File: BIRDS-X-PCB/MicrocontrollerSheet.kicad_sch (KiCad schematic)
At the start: 30 parts, among them J401 Conn_02x04_Odd_Even, J402 Conn_01x08, Q401 BSS138, Q402 BSS138, SW401 SW_Push, U401 STM32G031K8Tx, U402 MTT4B-Mini, U403 MT29F2G01ABAGDWB-IT-G_TR, Y401 ECS-2520SMV-080-FN-TR

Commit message: Add notes from schematic review session
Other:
- note added: "TODO breakout ~3 GPIOs, add debug LED"
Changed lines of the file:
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@@
+    (effects (font (size 1.27 1.27)) (justify left bottom))
+  )
+  (text "TODO breakout ~3 GPIOs, add debug LED" (at 184.15 102.87 0)
     (effects (font (size 1.27 1.27)) (justify left bottom))
   )

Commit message: Finish layout
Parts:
- added D203: LED, LED_SMD:LED_1206_3216Metric_Pad1.42x1.75mm_HandSolder, symbol Device:LED
- added J403: Conn_01x02, Connector_PinHeader_2.54mm:PinHeader_1x02_P2.54mm_Vertical, symbol Connector_Generic:Conn_01x02
- added J404: MHDR2X5, Connector_PinHeader_1.27mm:PinHeader_2x05_P1.27mm_Vertical_SMD, symbol Connector_Generic:Conn_02x05_Odd_Even
- added R205: R, Resistor_SMD:R_0805_2012Metric_Pad1.20x1.40mm_HandSolder, symbol Device:R
- C401, C402, C403, C404, C405, C406, C407, C408: footprint Capacitor_SMD:C_1206_3216Metric_Pad1.33x1.80mm_HandSolder -> Capacitor_SMD:C_0805_2012Metric_Pad1.18x1.45mm_HandSolder
- J401: value Conn_02x04_Odd_Even -> Conn_01x04; footprint Connector_PinSocket_2.54mm:PinSocket_2x04_P2.54mm_Vertical -> Connector_PinHeader_2.54mm:PinHeader_1x04_P2.54mm_Vertical; symbol Connector_Generic:Conn_02x04_Odd_Even -> Connector_Generic:Conn_01x04
- R401, R402, R403, R404, R405, R406, R407, R408, R409: footprint Resistor_SMD:R_1206_3216Metric_Pad1.30x1.75mm_HandSolder -> Resistor_SMD:R_0805_2012Metric_Pad1.20x1.40mm_HandSolder
- TP401: footprint TestPoint:TestPoint_Pad_D2.5mm -> TestPoint:TestPoint_Pad_D2.0mm
- U402: footprint BIRDS-X_Footprints_Lib:MTT4B-Mini -> BIRDS-X_Footprints_Lib:MTT4B-Mini_CanUp
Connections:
- net +3V3: now also J404.1 (Pin_1)
- net +5V: now also J401.3 (Pin_3); no longer J401.5 (Pin_5), J401.6 (Pin_6)
- net BOOT0: now also J404.4 (Pin_4)
- net GND: now also D203.1 (K), J404.3 (Pin_3), J404.5 (Pin_5), J404.9 (Pin_9); no longer J401.2 (Pin_2)
- net at JP403.1 (A), Q401.3 (D), R405.2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: now also J401.2 (Pin_2); no longer J401.3 (Pin_3), J401.4 (Pin_4)
- net at JP404.1 (A), Q402.3 (D), R406.2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: now also J401.4 (Pin_4); no longer J401.7 (Pin_7), J401.8 (Pin_8)
- net ST_RST: now reaches C401.1, SW401.2, U401.6 (PF2)
- net ST_RST: now also J404.10 (Pin_10)
- net at U401.22 (PA11/PA9): now also R205.1
- net at U401.23 (PA12/PA10): now also J403.1 (Pin_1)
- net ST_SWDIO: now reaches U401.24 (PA13)
- net ST_SWDIO: now also J404.2 (Pin_2)
- net at U401.26 (PA15): now also J403.2 (Pin_2)
- new net: D203.2 (A), R205.2
- no-connect marks 10 -> 9
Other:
- note added: "Breakout (at 5V logic)"
- note added: "Debugging"
- note added: "GP Debugging Breakout"
- note added: "ST-LINK/V2 Connector for Programming"
- note removed: "TODO add programming header from Iris schematic"
- note removed: "TODO breakout ~3 GPIOs, add debug LED"

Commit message: PCB update
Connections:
- net +3V3: no longer C404.1
- net GND: no longer C404.2
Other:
- moved on the sheet: C404
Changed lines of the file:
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@@
     )
   )
-  (symbol (lib_id "Device:C") (at 33.02 92.71 0) (unit 1)
+  (symbol (lib_id "Device:C") (at 33.02 92.71 90) (unit 1)
     (in_bom yes) (on_board yes) (dnp no)
-    (property "Reference" "C404" (at 35.56 91.44 0)
+    (property "Reference" "C404" (at 31.75 90.17 0)
       (effects (font (size 1.27 1.27)) (justify left))
     )
-    (property "Value" "10n" (at 35.56 93.98 0)
+    (property "Value" "10n" (at 34.29 90.17 0)
       (effects (font (size 1.27 1.27)) (justify left))
     )
-    (property "Footprint" "Capacitor_SMD:C_0805_2012Metric_Pad1.18x1.45mm_HandSolder" (at 33.9852 96.52 0)
+    (property "Footprint" "Capacitor_SMD:C_0805_2012Metric_Pad1.18x1.45mm_HandSolder" (at 36.83 91.7448 0)
       (effects (font (size 1.27 1.27)) hide)
     )

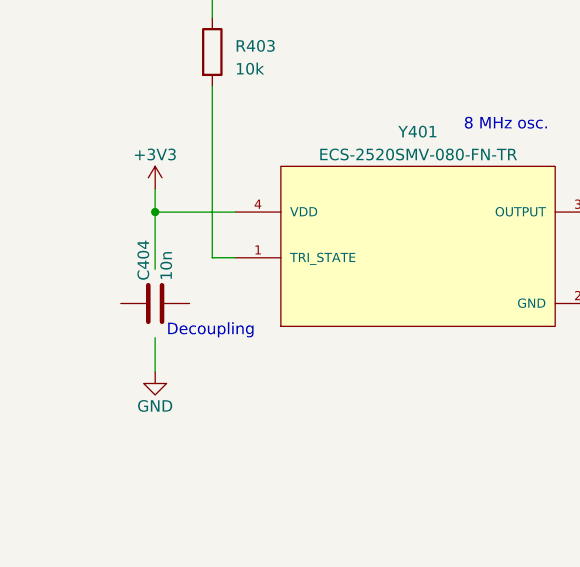
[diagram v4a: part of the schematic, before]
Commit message: Route power lines on 2-layer board, if desired
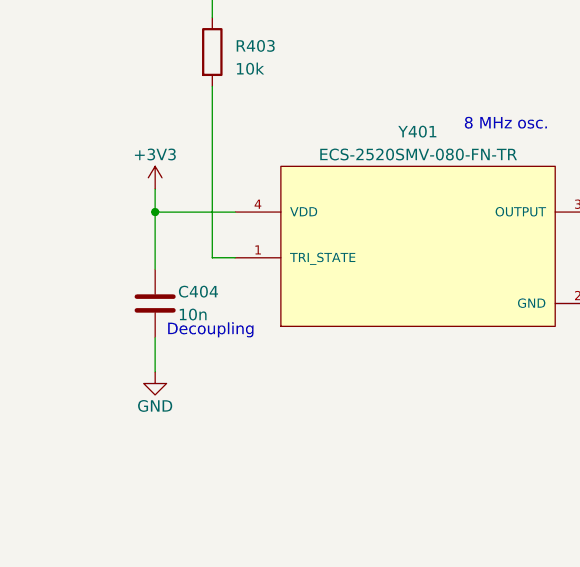
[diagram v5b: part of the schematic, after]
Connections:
- net +3V3: now also C404.1
- net GND: now also C404.2
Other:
- moved on the sheet: C404
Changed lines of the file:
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@@
     )
   )
-  (symbol (lib_id "Device:C") (at 33.02 92.71 90) (unit 1)
+  (symbol (lib_id "Device:C") (at 33.02 92.71 0) (unit 1)
     (in_bom yes) (on_board yes) (dnp no)
-    (property "Reference" "C404" (at 31.75 90.17 0)
+    (property "Reference" "C404" (at 35.56 91.44 0)
       (effects (font (size 1.27 1.27)) (justify left))
     )
-    (property "Value" "10n" (at 34.29 90.17 0)
+    (property "Value" "10n" (at 35.56 93.98 0)
       (effects (font (size 1.27 1.27)) (justify left))
     )
-    (property "Footprint" "Capacitor_SMD:C_0805_2012Metric_Pad1.18x1.45mm_HandSolder" (at 36.83 91.7448 0)
+    (property "Footprint" "Capacitor_SMD:C_0805_2012Metric_Pad1.18x1.45mm_HandSolder" (at 33.9852 96.52 0)
       (effects (font (size 1.27 1.27)) hide)
     )

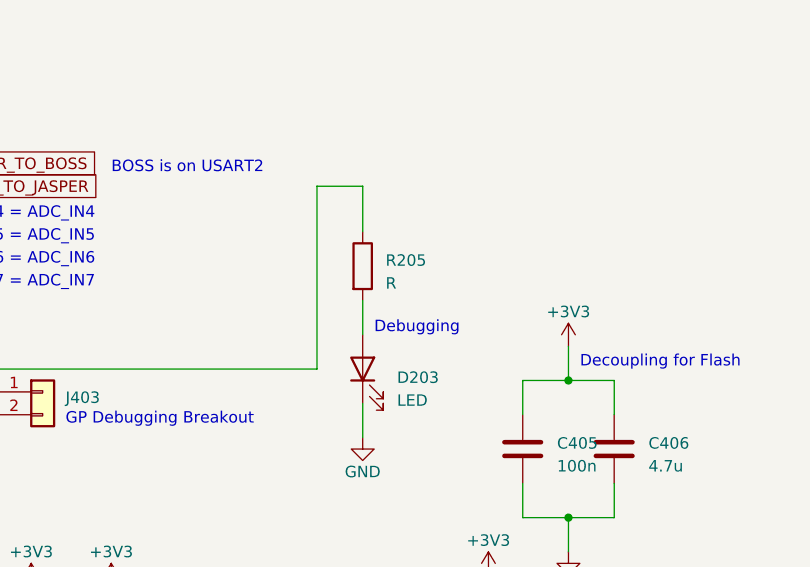
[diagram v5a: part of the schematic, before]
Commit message: Update resistor vals, plot, BOM
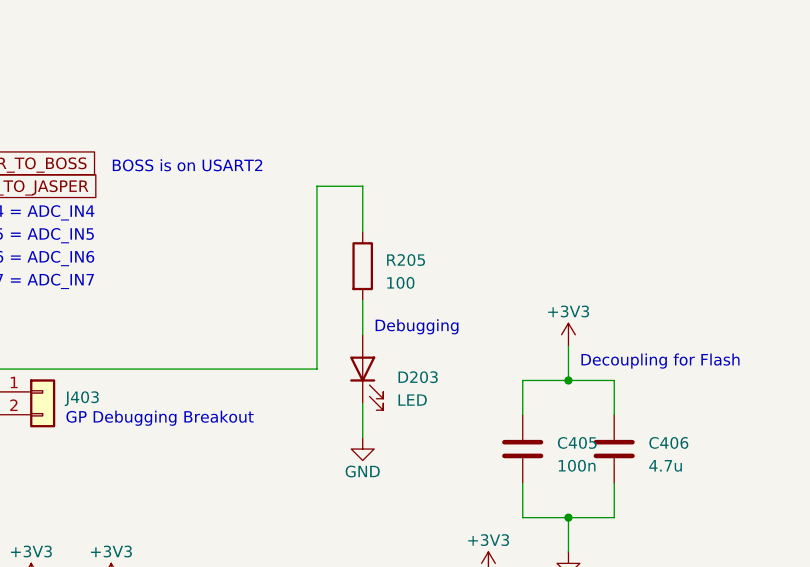
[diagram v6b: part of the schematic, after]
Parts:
- J402: footprint Connector_PinSocket_2.54mm:PinSocket_1x08_P2.54mm_Vertical -> Connector_PinHeader_2.54mm:PinHeader_1x08_P2.54mm_Vertical
- R205: value R -> 100
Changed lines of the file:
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@@
       (effects (font (size 1.27 1.27)) (justify left) hide)
     )
-    (property "Footprint" "Connector_PinSocket_2.54mm:PinSocket_1x08_P2.54mm_Vertical" (at 245.11 143.51 0)
+    (property "Footprint" "Connector_PinHeader_2.54mm:PinHeader_1x08_P2.54mm_Vertical" (at 245.11 143.51 0)
       (effects (font (size 1.27 1.27)) hide)
     )
@@
       (effects (font (size 1.27 1.27)) (justify left))
     )
-    (property "Value" "R" (at 220.98 93.345 0)
+    (property "Value" "100" (at 220.98 93.345 0)
       (effects (font (size 1.27 1.27)) (justify left))
     )

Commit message: Final changes for rev1
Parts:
- SW401: footprint Button_Switch_SMD:SW_Push_SPST_NO_Alps_SKRK -> Button_Switch_SMD:SW_Tactile_SPST_NO_Straight_CK_PTS636Sx25SMTRLFS
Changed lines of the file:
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@@
       (effects (font (size 1.27 1.27)) (justify right))
     )
-    (property "Footprint" "Button_Switch_SMD:SW_Push_SPST_NO_Alps_SKRK" (at 91.44 64.77 0)
+    (property "Footprint" "Button_Switch_SMD:SW_Tactile_SPST_NO_Straight_CK_PTS636Sx25SMTRLFS" (at 91.44 64.77 0)
       (effects (font (size 1.27 1.27)) hide)
     )

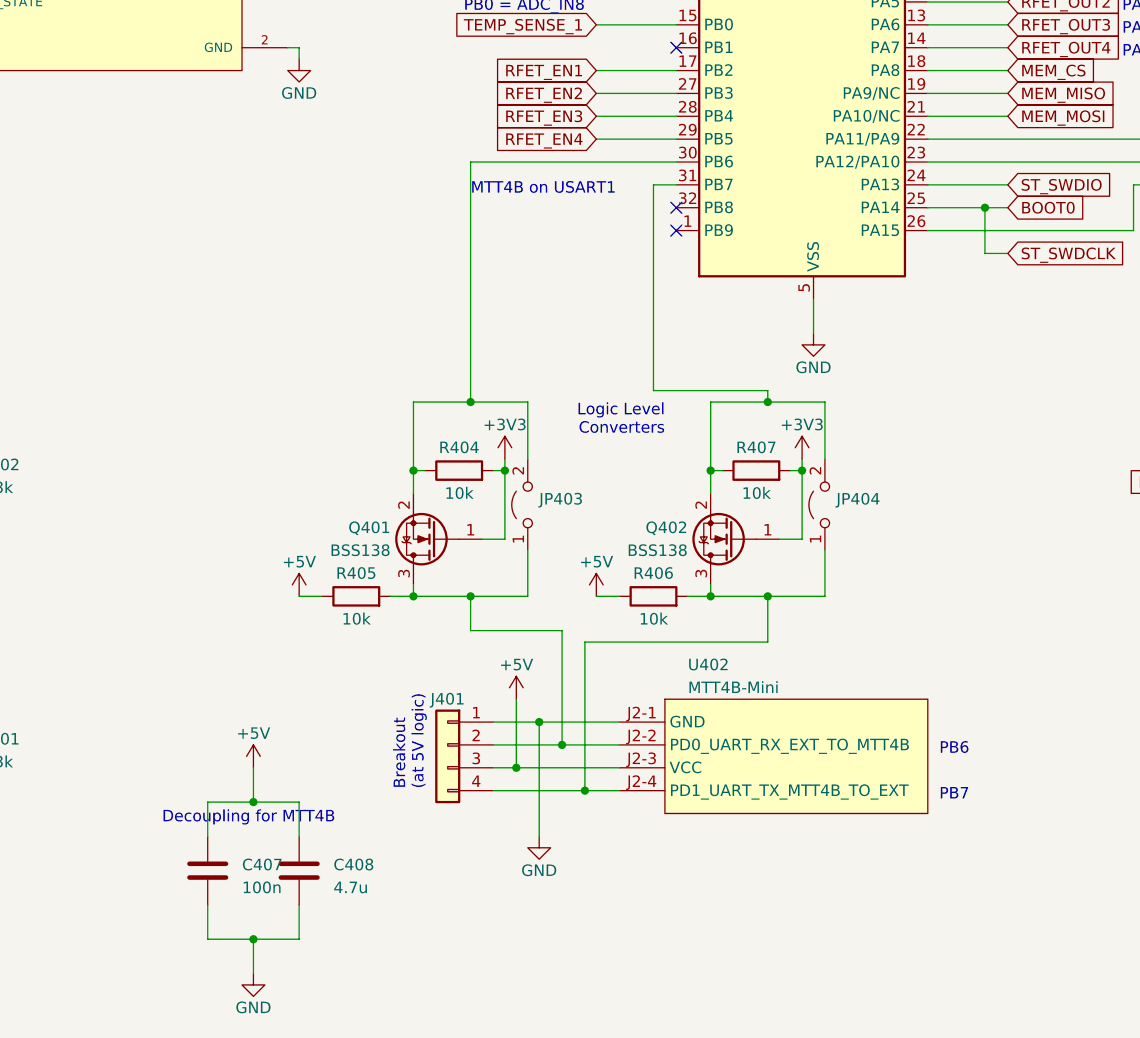
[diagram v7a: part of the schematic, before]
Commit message: Update footprints to 0603
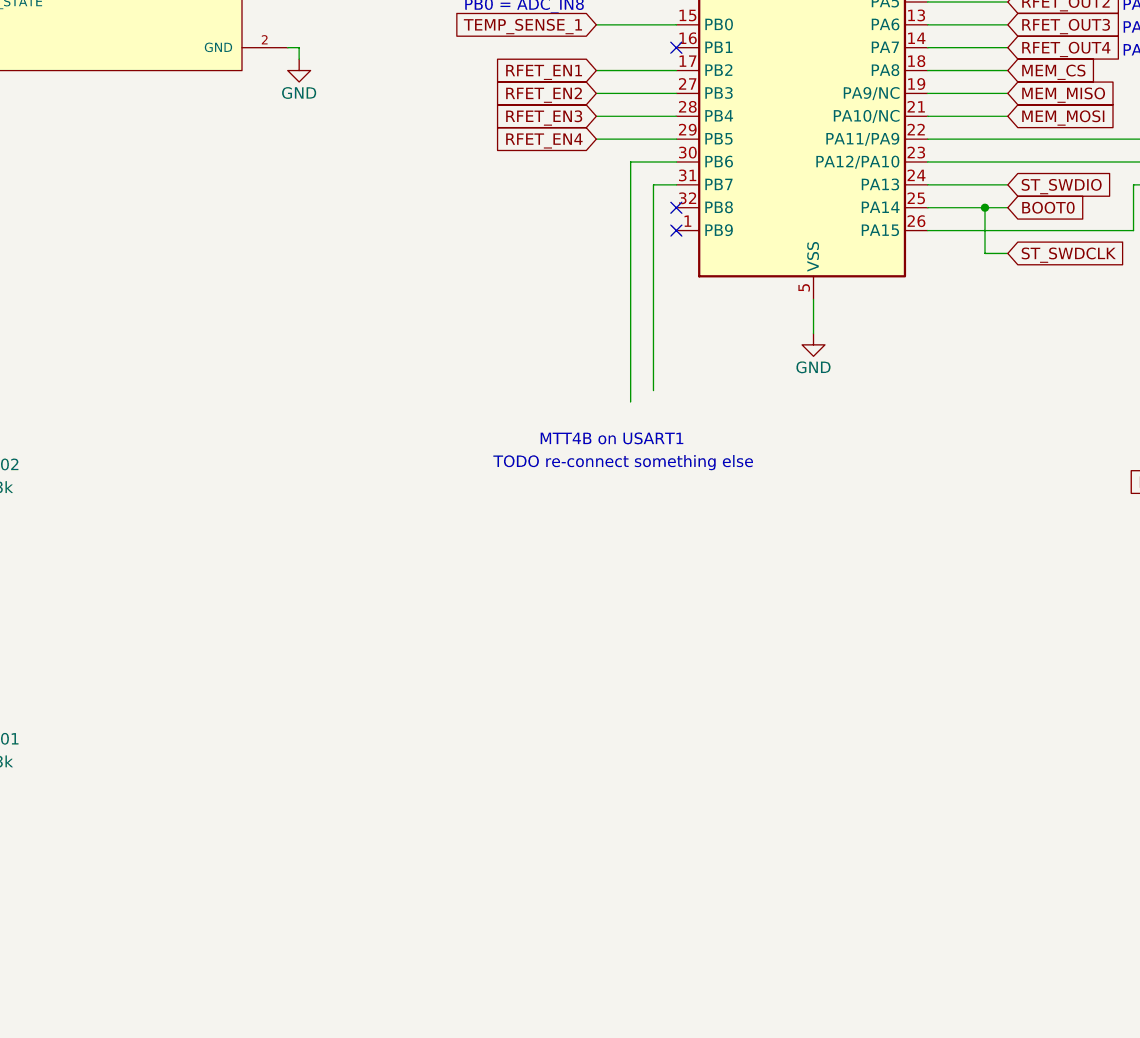
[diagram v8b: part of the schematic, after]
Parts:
- removed C407: 100n, Capacitor_SMD:C_0805_2012Metric_Pad1.18x1.45mm_HandSolder, symbol Device:C
- removed C408: 4.7u, Capacitor_SMD:C_0805_2012Metric_Pad1.18x1.45mm_HandSolder, symbol Device:C
- removed J401: Conn_01x04, Connector_PinHeader_2.54mm:PinHeader_1x04_P2.54mm_Vertical, symbol Connector_Generic:Conn_01x04
- removed JP403, JP404: Jumper_2_Open, Jumper:SolderJumper-2_P1.3mm_Open_RoundedPad1.0x1.5mm, symbol Jumper:Jumper_2_Open
- removed Q401, Q402: BSS138, Package_TO_SOT_SMD:SOT-23, symbol Transistor_FET:BSS138
- removed R404, R405, R406, R407: 10k, Resistor_SMD:R_0805_2012Metric_Pad1.20x1.40mm_HandSolder, symbol Device:R
- removed U402: MTT4B-Mini, BIRDS-X_Footprints_Lib:MTT4B-Mini_CanUp, symbol BIRDS-X_Symbols_Lib:MTT4B-Mini
- C401, C402, C403, C404, C405, C406: footprint Capacitor_SMD:C_0805_2012Metric_Pad1.18x1.45mm_HandSolder -> Capacitor_SMD:C_0603_1608Metric_Pad1.08x0.95mm_HandSolder
- J402: footprint Connector_PinHeader_2.54mm:PinHeader_1x08_P2.54mm_Vertical -> Connector_PinHeader_1.27mm:PinHeader_1x08_P1.27mm_Vertical
- J403: footprint Connector_PinHeader_2.54mm:PinHeader_1x02_P2.54mm_Vertical -> Connector_PinHeader_1.27mm:PinHeader_1x02_P1.27mm_Vertical
- R205, R401, R402, R403, R408, R409: footprint Resistor_SMD:R_0805_2012Metric_Pad1.20x1.40mm_HandSolder -> Resistor_SMD:R_0603_1608Metric_Pad0.98x0.95mm_HandSolder
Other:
- note added: "TODO re-connect something else"
- note removed: "Breakout (at 5V logic)"
- note removed: "Decoupling for MTT4B"
- note removed: "Logic Level Converters"
- note removed: "PB6"
- note removed: "PB7"
